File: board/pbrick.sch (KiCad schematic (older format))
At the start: 59 parts, among them J1 UJC-HP-3-SMT-TR, J2 TC2030-IDC-NL, J3 U.FL2PIN, J4 QWIIC, M0 5055680471, M1 5055680471, Q1 SSM6J507NU, Q2 SSM6J507NU, U1 MIC5219-3.3YML-TR, U2 ADP3330ARTZ-5-RL7, U3 STUSB4500QTR, U5 TB67H420FTG(O,EL), U6 2533020201601, U7 PCA9624

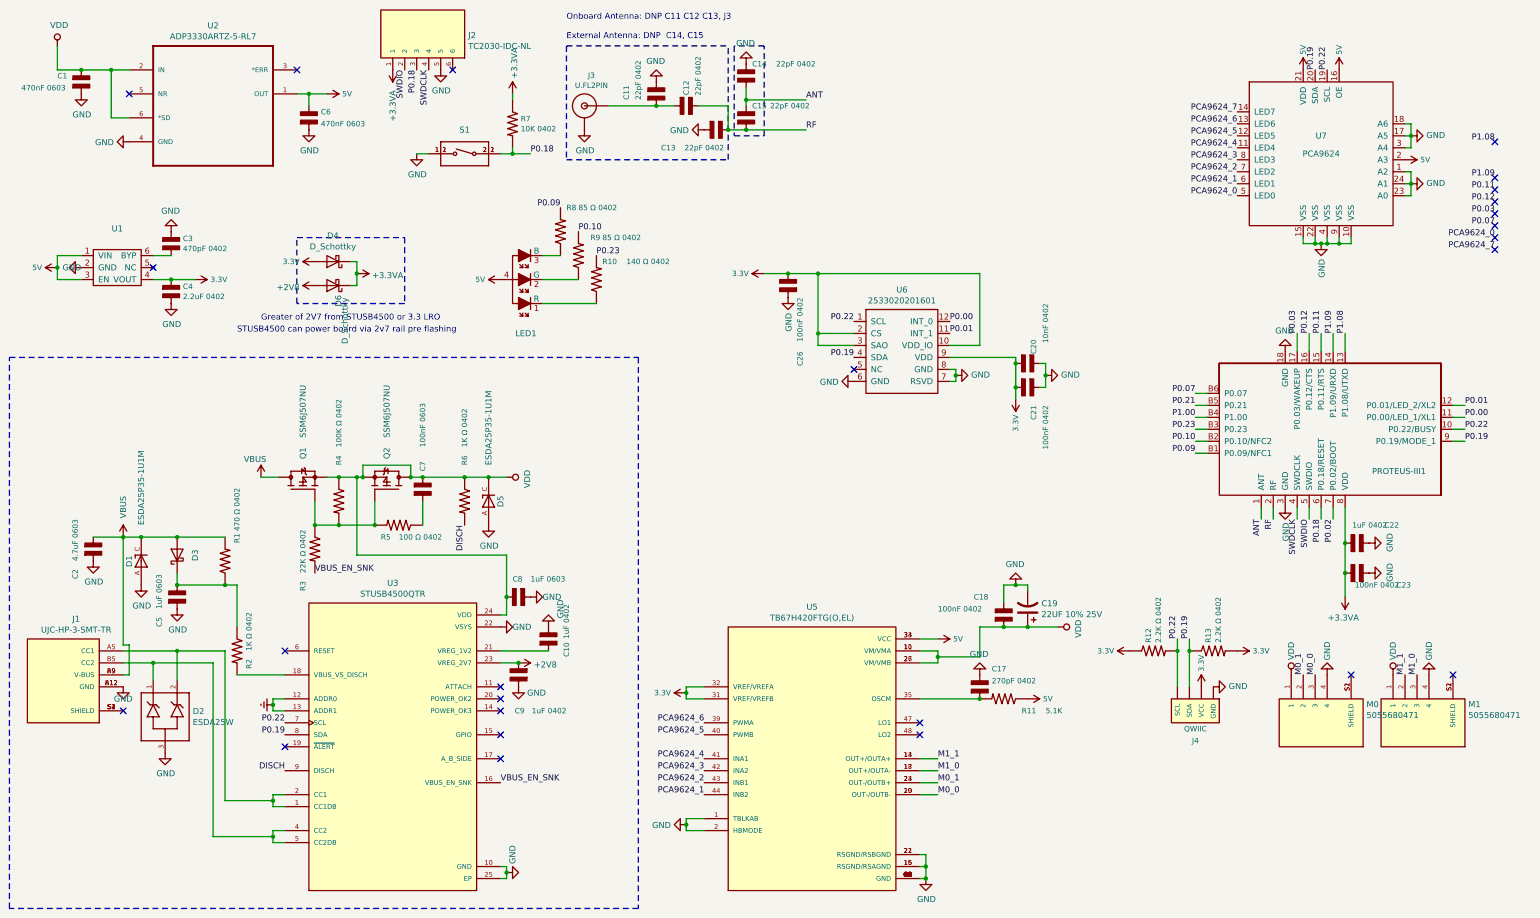
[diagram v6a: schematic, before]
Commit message: 5v regulator has operational capacity from 2.7-20v (tested)   - removing extra diode and 2.7v line as 5v => 3.3v works at 5v input
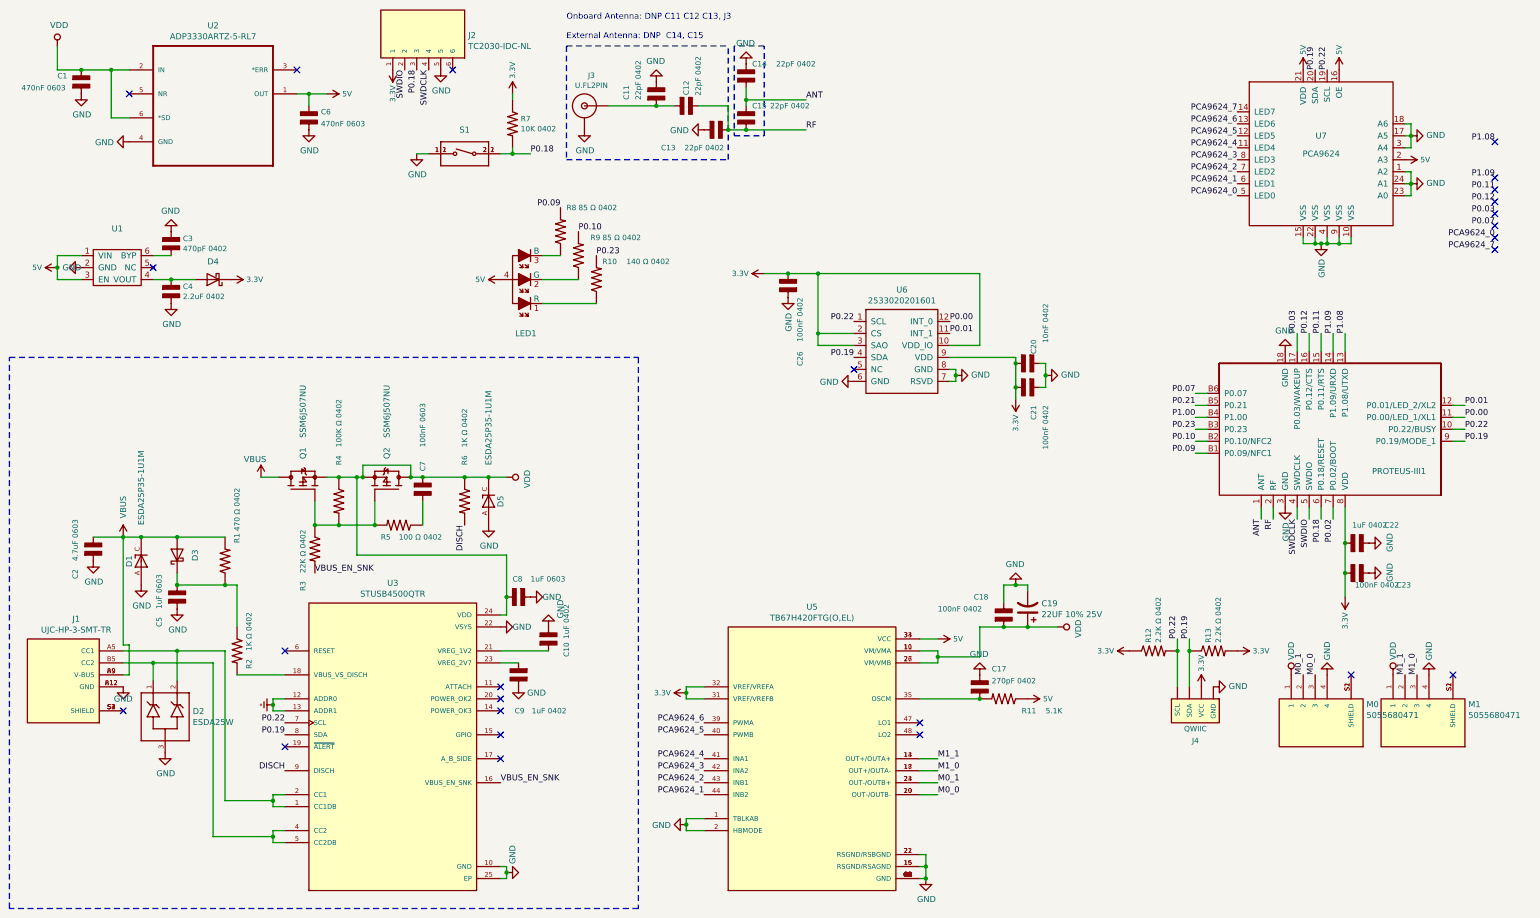
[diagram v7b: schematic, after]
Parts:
- removed D6: D_Schottky, Diode_SMD:D_0402_1005Metric, symbol Device:D_Schottky
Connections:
- net +3.3VA is gone; now on net 3.3V: C22.1, C23.1, D4.1 (K), J2.1, PROTEUS-III1.8 (VDD), R7.1
- net 3.3V: no longer C4.1, D4.2 (A), U1.4 (VOUT)
- net +2V8: no longer names the net of C9.2, U3.23 (VREG_2V7)
- new net: C4.1, D4.2 (A), U1.4 (VOUT)
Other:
- note removed: "Greater of 2V7 from STUSB4500 or 3.3 LRO\n"
- note removed: "STUSB4500 can power board via 2v7 rail pre flashing"
- moved on the sheet: D4
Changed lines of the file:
@@
 Text Label 5350 2600 0    50   ~ 0
 P0.23
-$Comp
-L pbrick-rescue:3.3V-SparkFun-PowerSymbols #SUPPLY02
-U 1 1 5F226DE7
-P 2000 2800
-F 0 "#SUPPLY02" H 2050 2800 45  0001 L BNN
-F 1 "3.3V" V 2000 2928 45  0000 L CNN
-F 2 "XXX-00000" V 1958 2927 60  0001 L CNN
-F 3 "" H 2000 2800 60  0001 C CNN
-	1    2000 2800
-	0    1    1    0
-$EndComp
 Wire Wire Line
 	2000 2800 1800 2800
@@
 	3350 4450 3200 4450
 $Comp
-L Device:D_Schottky D6
-U 1 1 60193B83
-P 3150 2850
-F 0 "D6" V 3104 2929 50  0000 L CNN
-F 1 "D_Schottky" V 3050 2950 50  0000 L CNN
-F 2 "Diode_SMD:D_0402_1005Metric" H 3150 2850 50  0001 C CNN
-F 3 "~" H 3150 2850 50  0001 C CNN
-F 4 "641-1675-1-ND" V 3150 2850 50  0001 C CNN "Digi-Key_PN"
-F 5 "Comchip Technology" V 3150 2850 50  0001 C CNN "Manufacturer"
-F 6 "CDBQR0130L-HF" V 3150 2850 50  0001 C CNN "MPN"
-F 7 "DIODE SCHOTTKY 30V 100MA 0402" V 3150 2850 50  0001 C CNN "Description"
-	1    3150 2850
-	-1   0    0    1
-$EndComp
-$Comp
 L pbrick-rescue:CAPACITOR_NP_0603-MF_Passives C10
 U 1 1 6028C11A
@@
 Wire Wire Line
 	4550 5900 4950 5900
-$Comp
-L Device:D_Schottky D4
-U 1 1 601C167B
-P 3150 2650
-F 0 "D4" H 3150 2434 50  0000 C CNN
-F 1 "D_Schottky" H 3150 2525 50  0000 C CNN
-F 2 "Diode_SMD:D_0402_1005Metric" H 3150 2650 50  0001 C CNN
-F 3 "~" H 3150 2650 50  0001 C CNN
-F 4 "641-1675-1-ND" V 3150 2650 50  0001 C CNN "Digi-Key_PN"
-F 5 "Comchip Technology" V 3150 2650 50  0001 C CNN "Manufacturer"
-F 6 "CDBQR0130L-HF" V 3150 2650 50  0001 C CNN "MPN"
-F 7 "DIODE SCHOTTKY 30V 100MA 0402" V 3150 2650 50  0001 C CNN "Description"
-	1    3150 2650
-	-1   0    0    1
-$EndComp
-$Comp
-L pbrick-rescue:3.3V-SparkFun-PowerSymbols #SUPPLY04
-U 1 1 601C2C68
-P 3000 2650
-F 0 "#SUPPLY04" H 3050 2650 45  0001 L BNN
-F 1 "3.3V" V 3000 2778 45  0000 L CNN
-F 2 "XXX-00000" V 2958 2777 60  0001 L CNN
-F 3 "" H 3000 2650 60  0001 C CNN
-	1    3000 2650
-	0    -1   -1   0
-$EndComp
-Wire Wire Line
-	3350 2850 3300 2850
-Wire Wire Line
-	3300 2650 3350 2650
-Wire Notes Line
-	2850 2450 3750 2450
-Wire Notes Line
-	3750 2450 3750 3000
-Wire Notes Line
-	3750 3000 2850 3000
-Wire Notes Line
-	2850 3000 2850 2450
-Text Notes 2550 3150 0    50   ~ 0
-Greater of 2V7 from STUSB4500 or 3.3 LRO\n
-Text Notes 2350 3250 0    50   ~ 0
-STUSB4500 can power board via 2v7 rail pre flashing
 $Comp
 L TC2030-IDC-NL:TC2030-IDC-NL J2
@@
 	1    0    0    -1
 $EndComp
-Connection ~ 4700 6000
 $Comp
 L power:GND #PWR0102
@@
 	1    4700 6200
 	1    0    0    -1
-$EndComp
-$Comp
-L power:+2V8 #PWR0103
-U 1 1 60392560
-P 4700 6000
-F 0 "#PWR0103" H 4700 5850 50  0001 C CNN
-F 1 "+2V8" V 4715 6128 50  0000 L CNN
-F 2 "" H 4700 6000 50  0001 C CNN
-F 3 "" H 4700 6000 50  0001 C CNN
-	1    4700 6000
-	0    1    1    0
-$EndComp
-$Comp
-L power:+2V8 #PWR0104
-U 1 1 60392933
-P 3000 2850
-F 0 "#PWR0104" H 3000 2700 50  0001 C CNN
-F 1 "+2V8" V 3015 2978 50  0000 L CNN
-F 2 "" H 3000 2850 50  0001 C CNN
-F 3 "" H 3000 2850 50  0001 C CNN
-	1    3000 2850
-	0    -1   1    0
-$EndComp
-$Comp
-L power:+3.3VA #PWR0105
-U 1 1 603A2D97
-P 3350 2750
-F 0 "#PWR0105" H 3350 2600 50  0001 C CNN
-F 1 "+3.3VA" V 3365 2878 50  0000 L CNN
-F 2 "" H 3350 2750 50  0001 C CNN
-F 3 "" H 3350 2750 50  0001 C CNN
-	1    3350 2750
-	0    1    1    0
-$EndComp
-Wire Wire Line
-	3350 2650 3350 2750
-Connection ~ 3350 2750
-Wire Wire Line
-	3350 2750 3350 2850
-$Comp
-L power:+3.3VA #PWR0106
-U 1 1 603A3842
-P 11600 5450
-F 0 "#PWR0106" H 11600 5300 50  0001 C CNN
-F 1 "+3.3VA" H 11615 5623 50  0000 C CNN
-F 2 "" H 11600 5450 50  0001 C CNN
-F 3 "" H 11600 5450 50  0001 C CNN
-	1    11600 5450
-	-1   0    0    1
 $EndComp
 $Comp
@@
 $EndComp
 $Comp
-L power:+3.3VA #PWR0114
-U 1 1 60522B8A
-P 3650 1050
-F 0 "#PWR0114" H 3650 900 50  0001 C CNN
-F 1 "+3.3VA" V 3650 1350 50  0000 C CNN
-F 2 "" H 3650 1050 50  0001 C CNN
-F 3 "" H 3650 1050 50  0001 C CNN
-	1    3650 1050
-	-1   0    0    1
-$EndComp
-$Comp
-L pbrick-rescue:3.3V-SparkFun-PowerSymbols #SUPPLY0102
-U 1 1 605C0668
-P 10400 6200
-F 0 "#SUPPLY0102" H 10450 6200 45  0001 L BNN
-F 1 "3.3V" V 10400 6328 45  0000 L CNN
-F 2 "XXX-00000" V 10358 6327 60  0001 L CNN
-F 3 "" H 10400 6200 60  0001 C CNN
-	1    10400 6200
-	1    0    0    -1
-$EndComp
-$Comp
 L pbrick-rescue:3.3V-SparkFun-PowerSymbols #SUPPLY0103
 U 1 1 605C136D
@@
 $EndComp
 $Comp
-L power:+3.3VA #PWR0112
-U 1 1 60491C73
-P 4650 1250
-F 0 "#PWR0112" H 4650 1100 50  0001 C CNN
-F 1 "+3.3VA" V 4665 1378 50  0000 L CNN
-F 2 "" H 4650 1250 50  0001 C CNN
-F 3 "" H 4650 1250 50  0001 C CNN
-	1    4650 1250
-	1    0    0    -1
-$EndComp
-$Comp
 L pbrick-rescue:CAPACITOR_NP_0603-MF_Passives C17
 U 1 1 5FEC1666
@@
 Connection ~ 3400 4450
 Connection ~ 3800 4450
+$Comp
+L pbrick-rescue:3.3V-SparkFun-PowerSymbols #SUPPLY0102
+U 1 1 605C0668
+P 10400 6200
+F 0 "#SUPPLY0102" H 10450 6200 45  0001 L BNN
+F 1 "3.3V" V 10400 6328 45  0000 L CNN
+F 2 "XXX-00000" V 10358 6327 60  0001 L CNN
+F 3 "" H 10400 6200 60  0001 C CNN
+	1    10400 6200
+	1    0    0    -1
+$EndComp
+$Comp
+L Device:D_Schottky D4
+U 1 1 601C167B
+P 2150 2800
+F 0 "D4" H 2150 2650 50  0000 C CNN
+F 1 "D_Schottky" H 1900 2650 50  0001 C CNN
+F 2 "Diode_SMD:D_0402_1005Metric" H 2150 2800 50  0001 C CNN
+F 3 "~" H 2150 2800 50  0001 C CNN
+F 4 "641-1675-1-ND" V 2150 2800 50  0001 C CNN "Digi-Key_PN"
+F 5 "Comchip Technology" V 2150 2800 50  0001 C CNN "Manufacturer"
+F 6 "CDBQR0130L-HF" V 2150 2800 50  0001 C CNN "MPN"
+F 7 "DIODE SCHOTTKY 30V 100MA 0402" V 2150 2800 50  0001 C CNN "Description"
+	1    2150 2800
+	-1   0    0    1
+$EndComp
+$Comp
+L pbrick-rescue:3.3V-SparkFun-PowerSymbols #SUPPLY0107
+U 1 1 60514EA3
+P 11600 5450
+F 0 "#SUPPLY0107" H 11650 5450 45  0001 L BNN
+F 1 "3.3V" V 11600 5578 45  0000 L CNN
+F 2 "XXX-00000" V 11558 5577 60  0001 L CNN
+F 3 "" H 11600 5450 60  0001 C CNN
+	1    11600 5450
+	-1   0    0    1
+$EndComp
+$Comp
+L pbrick-rescue:3.3V-SparkFun-PowerSymbols #SUPPLY0109
+U 1 1 6051A54D
+P 3650 1050
+F 0 "#SUPPLY0109" H 3700 1050 45  0001 L BNN
+F 1 "3.3V" V 3650 1178 45  0000 L CNN
+F 2 "XXX-00000" V 3608 1177 60  0001 L CNN
+F 3 "" H 3650 1050 60  0001 C CNN
+	1    3650 1050
+	-1   0    0    1
+$EndComp
+$Comp
+L pbrick-rescue:3.3V-SparkFun-PowerSymbols #SUPPLY0110
+U 1 1 60531E6C
+P 4650 1250
+F 0 "#SUPPLY0110" H 4700 1250 45  0001 L BNN
+F 1 "3.3V" V 4650 1378 45  0000 L CNN
+F 2 "XXX-00000" V 4608 1377 60  0001 L CNN
+F 3 "" H 4650 1250 60  0001 C CNN
+	1    4650 1250
+	1    0    0    -1
+$EndComp
+$Comp
+L pbrick-rescue:3.3V-SparkFun-PowerSymbols #SUPPLY?
+U 1 1 6056102B
+P 2300 2800
+F 0 "#SUPPLY?" H 2350 2800 45  0001 L BNN
+F 1 "3.3V" V 2300 2928 45  0000 L CNN
+F 2 "XXX-00000" V 2258 2927 60  0001 L CNN
+F 3 "" H 2300 2800 60  0001 C CNN
+	1    2300 2800
+	0    1    1    0
+$EndComp
 $EndSCHEMATC

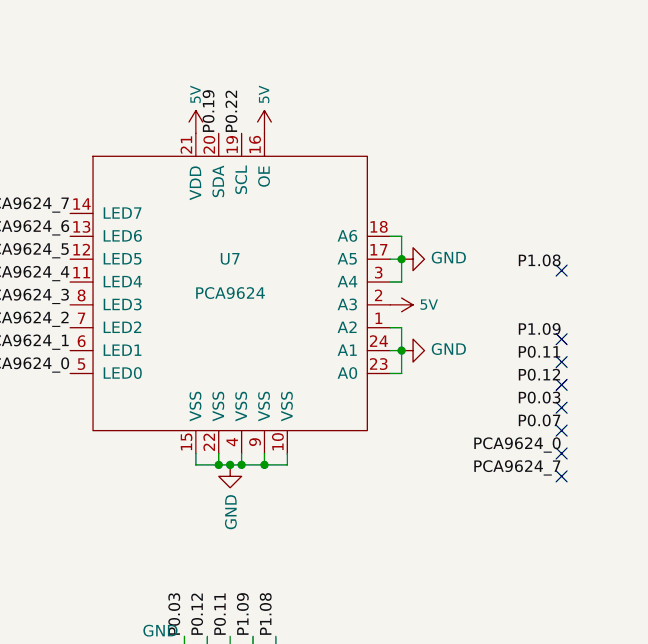
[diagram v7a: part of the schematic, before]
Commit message: Updating PCB to resolve an issue with PCA9624 OE being HIGH instead of Controller - Added PCA9624 library definition (untested) - Convert pbrick_motor to use PCA9624 driver
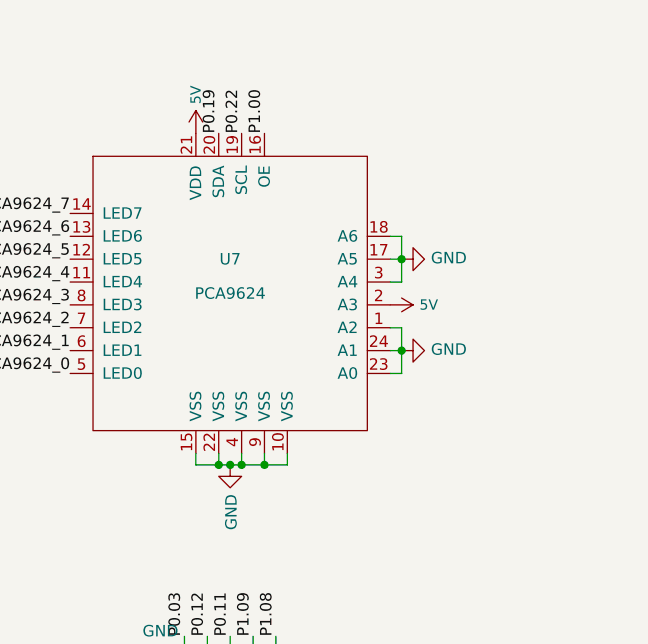
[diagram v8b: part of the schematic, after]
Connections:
- net 5V: no longer U7.16 (OE)
- net P1.00: now also U7.16 (OE)
- no-connect marks 25 -> 17
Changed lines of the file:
@@
 	1    0    0    -1
 $EndComp
-Text Label 12850 2050 2    50   ~ 0
-P0.11
-Text Label 12850 2150 2    50   ~ 0
-P0.12
-Text Label 12850 2250 2    50   ~ 0
-P0.03
-Text Label 12850 2350 2    50   ~ 0
-P0.07
 Wire Notes Line
 	450  3450 5700 3450
@@
 Text Label 10700 1400 2    50   ~ 0
 PCA9624_7
-NoConn ~ 12850 2050
-NoConn ~ 12850 2150
-NoConn ~ 12850 2250
-NoConn ~ 12850 2350
-Text Label 12850 1950 2    50   ~ 0
-P1.09
 Text Label 8300 3250 0    50   ~ 0
 P0.01
 Text Label 8300 3150 0    50   ~ 0
 P0.00
-NoConn ~ 12850 1950
-NoConn ~ 12850 2550
-NoConn ~ 12850 2450
 Connection ~ 10300 5900
 Wire Wire Line
@@
 	0    -1   -1   0
 $EndComp
-Text Label 12850 1650 2    50   ~ 0
-P1.08
-NoConn ~ 12850 1650
 $Comp
 L pbrick:2533020201601 U6
@@
 	1    0    0    -1
 $EndComp
-$Comp
-L pbrick-rescue:5V-SparkFun-PowerSymbols #SUPPLY0105
-U 1 1 603806F3
-P 11550 1050
-F 0 "#SUPPLY0105" H 11600 1050 45  0001 L BNN
-F 1 "5V" V 11550 1178 45  0000 L CNN
-F 2 "XXX-00000" V 11592 1178 60  0001 L CNN
-F 3 "" H 11550 1050 60  0001 C CNN
-	1    11550 1050
-	1    0    0    -1
-$EndComp
 Wire Wire Line
 	11650 2500 11650 2450
@@
 	1    0    0    -1
 $EndComp
-Text Label 12850 2450 2    50   ~ 0
-PCA9624_0
-Text Label 12850 2550 2    50   ~ 0
-PCA9624_7
 Wire Wire Line
 	3400 4450 3400 4350
@@
 $EndComp
 $Comp
-L pbrick-rescue:3.3V-SparkFun-PowerSymbols #SUPPLY?
+L pbrick-rescue:3.3V-SparkFun-PowerSymbols #SUPPLY0105
 U 1 1 6056102B
 P 2300 2800
-F 0 "#SUPPLY?" H 2350 2800 45  0001 L BNN
+F 0 "#SUPPLY0105" H 2350 2800 45  0001 L BNN
 F 1 "3.3V" V 2300 2928 45  0000 L CNN
 F 2 "XXX-00000" V 2258 2927 60  0001 L CNN
@@
 	0    1    1    0
 $EndComp
+Text Label 11550 1050 1    50   ~ 0
+P1.00
 $EndSCHEMATC
